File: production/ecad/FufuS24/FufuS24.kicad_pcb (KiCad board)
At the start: 4 copper layers, 120 x 120 mm, 137 parts, among them J1 Conn_01x02, J10 691137710002, J11 USB_B_Micro, J12 691137710002, J13 5033950410, J2 Conn_01x02, J3 691137710002, J4 Conn_01x12_Socket, J5 691137710004, J6 5025840270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

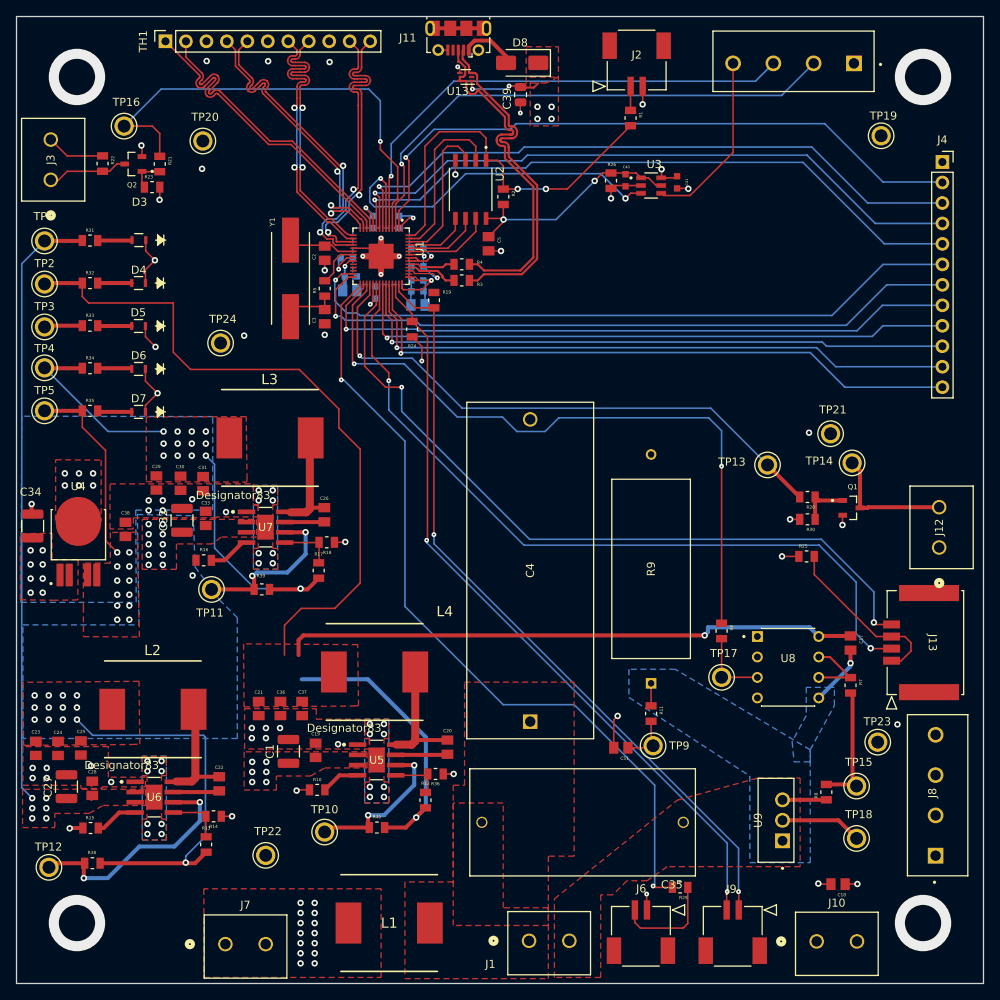
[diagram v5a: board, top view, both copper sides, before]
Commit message: fixed all design rules violations
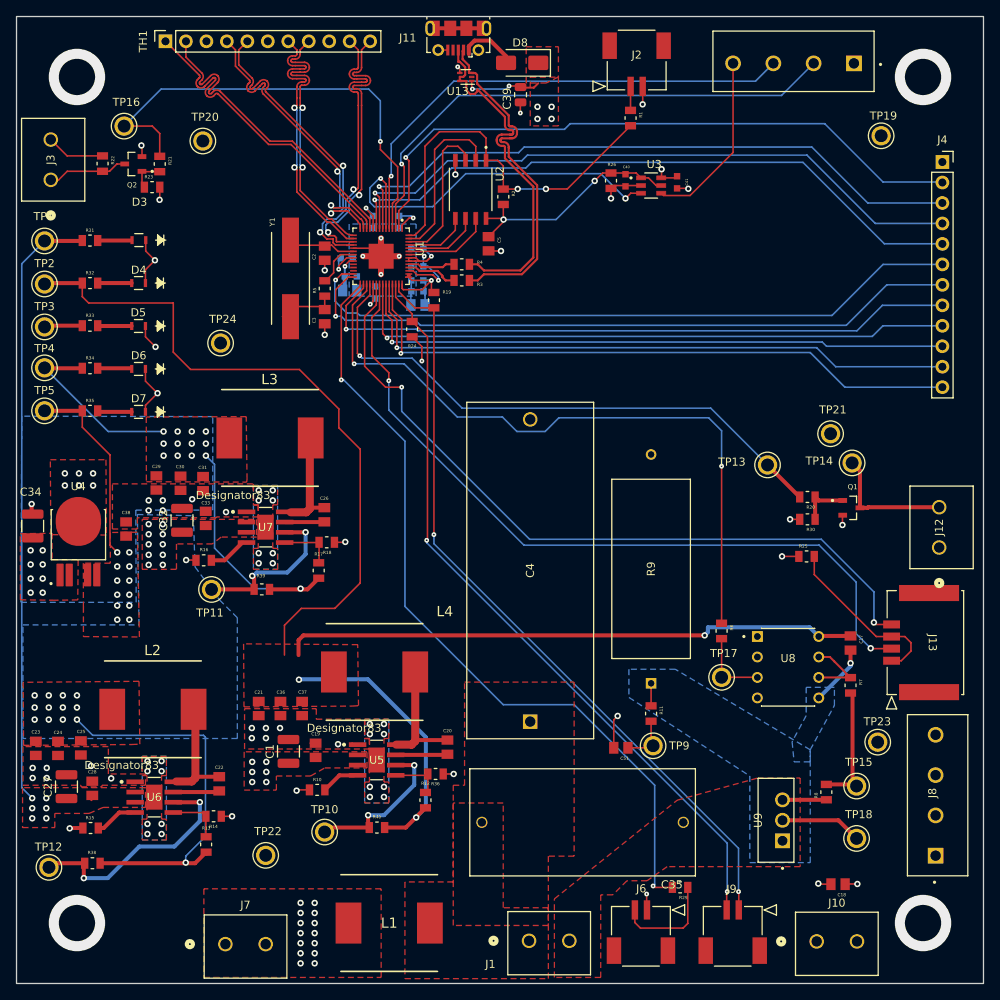
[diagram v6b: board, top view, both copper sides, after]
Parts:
- moved C38 0.09 mm to (93.6, 93.6)
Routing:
- net Net-(U1-VREG_VOUT): track 13.8 -> 24.8 mm
- net GNDREF: track 77.7 -> 80.0 mm, vias 89 -> 82
- net +3.3V: track 96.9 -> 94.8 mm
- net Net-(U6-SW): track 15.0 -> 13.9 mm
- net Net-(U1-XIN): track 9.39 -> 8.50 mm
- net Net-(U1-QSPI_SD2): track 18.6 -> 17.8 mm
- net +16V: vias 2 -> 3

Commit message: Fixed HDMI
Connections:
- U1 pad 11: DVI_CK+ -> DVI_D2+
- U1 pad 12: DVI_CK- -> DVI_D2-
- U1 pad 13: DVI_D0- -> DVI_D1+
- U1 pad 14: DVI_D0+ -> DVI_D1-
- U1 pad 15: DVI_D1+ -> DVI_D0+
- U1 pad 16: DVI_D1- -> DVI_D0-
- U1 pad 17: DVI_D2+ -> DVI_CK+
- U1 pad 18: DVI_D2- -> DVI_CK-
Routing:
- net DVI_CK+: track 39.8 -> 35.1 mm
- net DVI_CK-: track 40.6 -> 36.6 mm
- net Motor_PWM: track 47.2 -> 49.5 mm
- net GPIO_6: track 80.2 -> 82.4 mm
- net Motor_Direction: track 62.2 -> 63.9 mm
- net GPIO_4: track 80.2 -> 81.9 mm
- net GPIO_5: track 80.5 -> 82.1 mm
- net DVI_D0+: track 36.6 -> 35.0 mm, vias 2 -> 0
- net Piezo_Enable: track 59.0 -> 60.4 mm
- net DVI_D1-: track 36.3 -> 34.9 mm, vias 2 -> 0
- net DVI_D2+: track 36.2 -> 34.8 mm, vias 2 -> 0
- net Motor_Enable: track 65.8 -> 67.0 mm
- net GPIO_0: track 80.8 -> 81.9 mm
- net +3.3V: track 94.8 -> 95.8 mm
- net DVI_D2-: track 37.2 -> 36.3 mm, vias 2 -> 0
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
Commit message: silkscreen
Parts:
- moved J12 1.00 mm to (194.5, 94.9)
- moved R26 0.43 mm to (153.3, 50.4)
- moved C40 0.42 mm to (155.2, 50.3)
- moved R21 0.32 mm to (98.1, 48.3)
- moved TP16 0.25 mm to (93.3, 43.4)
